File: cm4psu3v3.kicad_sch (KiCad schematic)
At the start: 26 parts, among them U12 AP64501SP-13

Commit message: respin
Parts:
- renumbered C30 to C32, C31 to C33, C32 to C34, C33 to C35, C34 to C36, C35 to C37, C36 to C38, C37 to C39, C38 to C40, C39 to C41, C40 to C42, C41 to C43, C42 to C44, C43 to C45, C44 to C46, C45 to C47, D9 to D8, R34 to R37, R35 to R38, R36 to R39, R37 to R40, R38 to R41, U12 to U13
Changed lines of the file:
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@@
   (symbol (lib_id "Device:C_Small") (at 168.91 160.02 0) (unit 1)
     (in_bom yes) (on_board yes)
-    (property "Reference" "C37" (id 0) (at 171.45 158.75 0)
+    (property "Reference" "C39" (id 0) (at 171.45 158.75 0)
       (effects (font (size 1.27 1.27)) (justify left))
     )
@@
   (symbol (lib_id "Device:C_Small") (at 121.92 151.13 0) (unit 1)
     (in_bom yes) (on_board yes)
-    (property "Reference" "C33" (id 0) (at 124.46 149.86 0)
+    (property "Reference" "C35" (id 0) (at 124.46 149.86 0)
       (effects (font (size 1.27 1.27)) (justify left))
     )
@@
   (symbol (lib_id "power:GND") (at 152.4 171.45 0) (unit 1)
     (in_bom yes) (on_board yes)
-    (property "Reference" "#PWR037" (id 0) (at 152.4 177.8 0)
+    (property "Reference" "#PWR038" (id 0) (at 152.4 177.8 0)
       (effects (font (size 1.27 1.27)) hide)
     )
@@
   (symbol (lib_id "Capacitor_Tantalum_SMD_MyOwn:CP_EIA-7343-31_Kemet-D") (at 292.1 134.62 0) (unit 1)
     (in_bom yes) (on_board yes)
-    (property "Reference" "C45" (id 0) (at 294.64 133.35 0)
+    (property "Reference" "C47" (id 0) (at 294.64 133.35 0)
       (effects (font (size 1.27 1.27)) (justify left))
     )
@@
   (symbol (lib_id "Device:C_Small") (at 158.75 134.62 0) (unit 1)
     (in_bom yes) (on_board yes)
-    (property "Reference" "C36" (id 0) (at 161.29 133.35 0)
+    (property "Reference" "C38" (id 0) (at 161.29 133.35 0)
       (effects (font (size 1.27 1.27)) (justify left))
     )
@@
   (symbol (lib_id "Device:R_Small") (at 219.71 160.02 0) (unit 1)
     (in_bom yes) (on_board yes)
-    (property "Reference" "R37" (id 0) (at 220.98 158.75 0)
+    (property "Reference" "R40" (id 0) (at 220.98 158.75 0)
       (effects (font (size 1.27 1.27)) (justify left))
     )
@@
   (symbol (lib_id "Device:C_Small") (at 243.84 134.62 0) (unit 1)
     (in_bom yes) (on_board yes)
-    (property "Reference" "C41" (id 0) (at 246.38 133.35 0)
+    (property "Reference" "C43" (id 0) (at 246.38 133.35 0)
       (effects (font (size 1.27 1.27)) (justify left))
     )
@@
   (symbol (lib_id "Device:R_Small") (at 170.18 128.27 270) (unit 1)
     (in_bom yes) (on_board yes)
-    (property "Reference" "R34" (id 0) (at 168.91 125.73 90)
+    (property "Reference" "R37" (id 0) (at 168.91 125.73 90)
       (effects (font (size 1.27 1.27)) (justify left))
     )
@@
   (symbol (lib_id "Device:C_Small") (at 255.27 134.62 0) (unit 1)
     (in_bom yes) (on_board yes)
-    (property "Reference" "C42" (id 0) (at 257.81 133.35 0)
+    (property "Reference" "C44" (id 0) (at 257.81 133.35 0)
       (effects (font (size 1.27 1.27)) (justify left))
     )
@@
   (symbol (lib_id "Device:C_Small") (at 278.13 134.62 0) (unit 1)
     (in_bom yes) (on_board yes)
-    (property "Reference" "C44" (id 0) (at 280.67 133.35 0)
+    (property "Reference" "C46" (id 0) (at 280.67 133.35 0)
       (effects (font (size 1.27 1.27)) (justify left))
     )
@@
   (symbol (lib_id "LED_SMD_LiteOn:LED Green") (at 307.975 143.51 270) (unit 1)
     (in_bom yes) (on_board yes)
-    (property "Reference" "D9" (id 0) (at 311.15 142.875 90))
+    (property "Reference" "D8" (id 0) (at 311.15 142.875 90))
     (property "Value" "LED Green" (id 1) (at 314.96 144.78 90))
     (property "Footprint" "LED_SMD_LiteOn:LED_0603_1608Metric_green" (id 2) (at 297.815 143.51 0)
@@
   (symbol (lib_id "Device:C_Small") (at 227.33 137.16 0) (unit 1)
     (in_bom no) (on_board no)
-    (property "Reference" "C40" (id 0) (at 229.87 135.89 0)
+    (property "Reference" "C42" (id 0) (at 229.87 135.89 0)
       (effects (font (size 1.27 1.27)) (justify left))
     )
@@
   (symbol (lib_id "power:GND") (at 292.1 171.45 0) (unit 1)
     (in_bom yes) (on_board yes)
-    (property "Reference" "#PWR041" (id 0) (at 292.1 177.8 0)
+    (property "Reference" "#PWR042" (id 0) (at 292.1 177.8 0)
       (effects (font (size 1.27 1.27)) hide)
     )
@@
   (symbol (lib_id "Device:R_Small") (at 307.975 134.62 0) (unit 1)
     (in_bom yes) (on_board yes)
-    (property "Reference" "R38" (id 0) (at 311.15 133.35 0))
+    (property "Reference" "R41" (id 0) (at 311.15 133.35 0))
     (property "Value" "1k" (id 1) (at 311.15 135.89 0))
     (property "Footprint" "Resistor_SMD:R_0402_1005Metric" (id 2) (at 307.975 134.62 0)
@@
   (symbol (lib_id "Device:R_Small") (at 208.28 156.21 0) (unit 1)
     (in_bom yes) (on_board yes)
-    (property "Reference" "R35" (id 0) (at 209.55 154.94 0)
+    (property "Reference" "R38" (id 0) (at 209.55 154.94 0)
       (effects (font (size 1.27 1.27)) (justify left))
     )
@@
   (symbol (lib_id "Device:C_Small") (at 91.44 151.13 0) (unit 1)
     (in_bom yes) (on_board yes)
-    (property "Reference" "C31" (id 0) (at 93.98 149.86 0)
+    (property "Reference" "C33" (id 0) (at 93.98 149.86 0)
       (effects (font (size 1.27 1.27)) (justify left))
     )
@@
   (symbol (lib_id "Device:C_Small") (at 208.28 163.83 0) (unit 1)
     (in_bom yes) (on_board yes)
-    (property "Reference" "C39" (id 0) (at 210.82 162.56 0)
+    (property "Reference" "C41" (id 0) (at 210.82 162.56 0)
       (effects (font (size 1.27 1.27)) (justify left))
     )
@@
   (symbol (lib_id "Device:C_Small") (at 76.2 151.13 0) (unit 1)
     (in_bom yes) (on_board yes)
-    (property "Reference" "C30" (id 0) (at 78.74 149.86 0)
+    (property "Reference" "C32" (id 0) (at 78.74 149.86 0)
       (effects (font (size 1.27 1.27)) (justify left))
     )
@@
   (symbol (lib_id "power:GND") (at 307.975 171.45 0) (unit 1)
     (in_bom yes) (on_board yes)
-    (property "Reference" "#PWR042" (id 0) (at 307.975 177.8 0)
+    (property "Reference" "#PWR043" (id 0) (at 307.975 177.8 0)
       (effects (font (size 1.27 1.27)) hide)
     )
@@
   (symbol (lib_id "Device:C_Small") (at 266.7 134.62 0) (unit 1)
     (in_bom yes) (on_board yes)
-    (property "Reference" "C43" (id 0) (at 269.24 133.35 0)
+    (property "Reference" "C45" (id 0) (at 269.24 133.35 0)
       (effects (font (size 1.27 1.27)) (justify left))
     )
@@
   (symbol (lib_id "Device:C_Small") (at 137.16 151.13 0) (unit 1)
     (in_bom yes) (on_board yes)
-    (property "Reference" "C34" (id 0) (at 139.7 149.86 0)
+    (property "Reference" "C36" (id 0) (at 139.7 149.86 0)
       (effects (font (size 1.27 1.27)) (justify left))
     )
@@
   (symbol (lib_id "power:GND") (at 278.13 171.45 0) (unit 1)
     (in_bom yes) (on_board yes)
-    (property "Reference" "#PWR040" (id 0) (at 278.13 177.8 0)
+    (property "Reference" "#PWR041" (id 0) (at 278.13 177.8 0)
       (effects (font (size 1.27 1.27)) hide)
     )
@@
   (symbol (lib_id "Device:R_Small") (at 212.09 137.16 0) (unit 1)
     (in_bom yes) (on_board yes)
-    (property "Reference" "R36" (id 0) (at 213.36 135.89 0)
+    (property "Reference" "R39" (id 0) (at 213.36 135.89 0)
       (effects (font (size 1.27 1.27)) (justify left))
     )
@@
   (symbol (lib_id "Regulator_Switching_Diodes:AP64501SP-13") (at 177.8 147.32 0) (unit 1)
     (in_bom yes) (on_board yes)
-    (property "Reference" "U12" (id 0) (at 177.165 137.16 0))
+    (property "Reference" "U13" (id 0) (at 177.165 137.16 0))
     (property "Value" "AP64501SP-13" (id 1) (at 177.8 139.7 0))
     (property "Footprint" "Regulator_Switching_Diodes:SOIC-8-1EP_3.9x4.9mm_P1.27mm_EP2.95x4.9mm_Mask2.71x3.4mm_ThermalVias" (id 2) (at 177.8 172.72 0)
@@
   (symbol (lib_id "Device:C_Small") (at 106.68 151.13 0) (unit 1)
     (in_bom yes) (on_board yes)
-    (property "Reference" "C32" (id 0) (at 109.22 149.86 0)
+    (property "Reference" "C34" (id 0) (at 109.22 149.86 0)
       (effects (font (size 1.27 1.27)) (justify left))
     )
@@
   (symbol (lib_id "power:GND") (at 251.46 171.45 0) (unit 1)
     (in_bom yes) (on_board yes)
-    (property "Reference" "#PWR039" (id 0) (at 251.46 177.8 0)
+    (property "Reference" "#PWR040" (id 0) (at 251.46 177.8 0)
       (effects (font (size 1.27 1.27)) hide)
     )
@@
   (symbol (lib_id "Device:C_Small") (at 196.85 160.02 0) (unit 1)
     (in_bom yes) (on_board yes)
-    (property "Reference" "C38" (id 0) (at 199.39 158.75 0)
+    (property "Reference" "C40" (id 0) (at 199.39 158.75 0)
       (effects (font (size 1.27 1.27)) (justify left))
     )
@@
   (symbol (lib_id "power:GND") (at 219.71 171.45 0) (unit 1)
     (in_bom yes) (on_board yes)
-    (property "Reference" "#PWR038" (id 0) (at 219.71 177.8 0)
+    (property "Reference" "#PWR039" (id 0) (at 219.71 177.8 0)
       (effects (font (size 1.27 1.27)) hide)
     )
@@
   (symbol (lib_id "Device:C_Small") (at 152.4 151.13 0) (unit 1)
     (in_bom yes) (on_board yes)
-    (property "Reference" "C35" (id 0) (at 154.94 149.86 0)
-      (effects (font (size 1.27 1.27)) (justify left))
-    )
+    (property "Reference" "C37" (id 0) (at 154.94 149.86 0)
+      (effects (font (size 1.27 1.27)) (justify left))
+    )

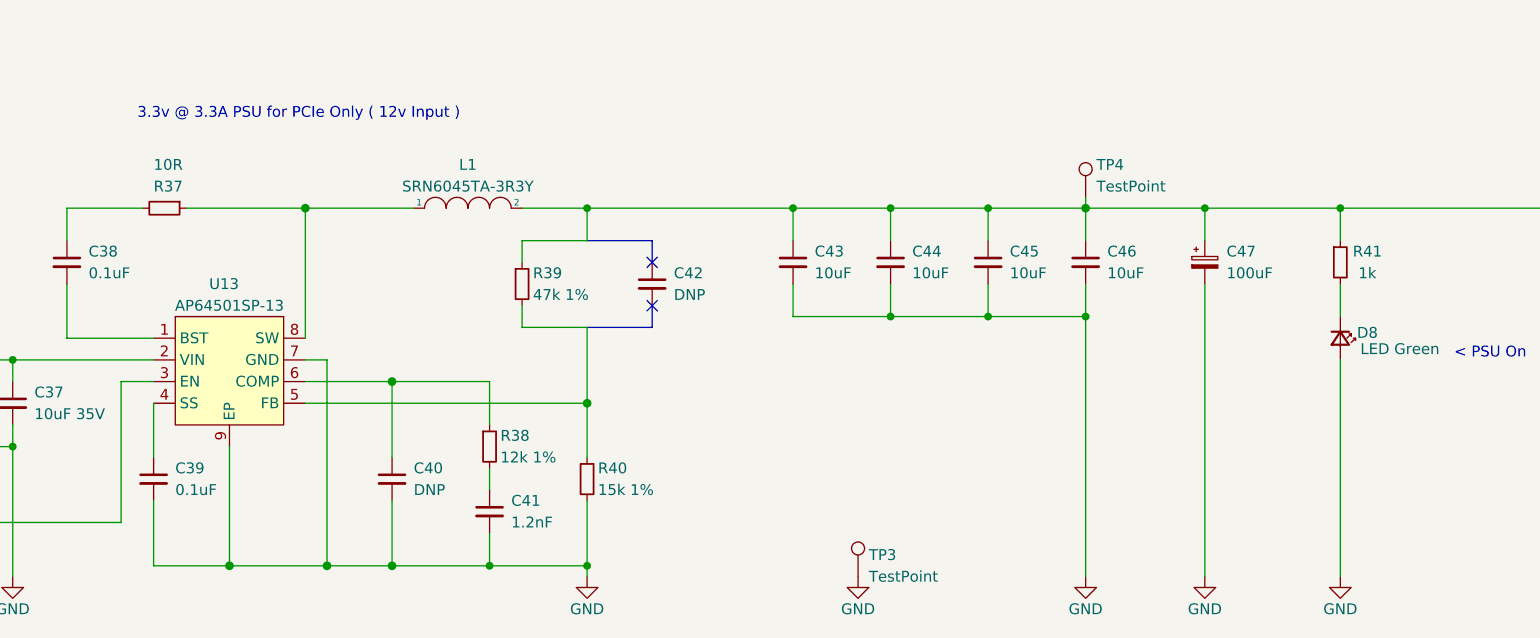
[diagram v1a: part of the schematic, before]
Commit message: fixed I2C ping indicator
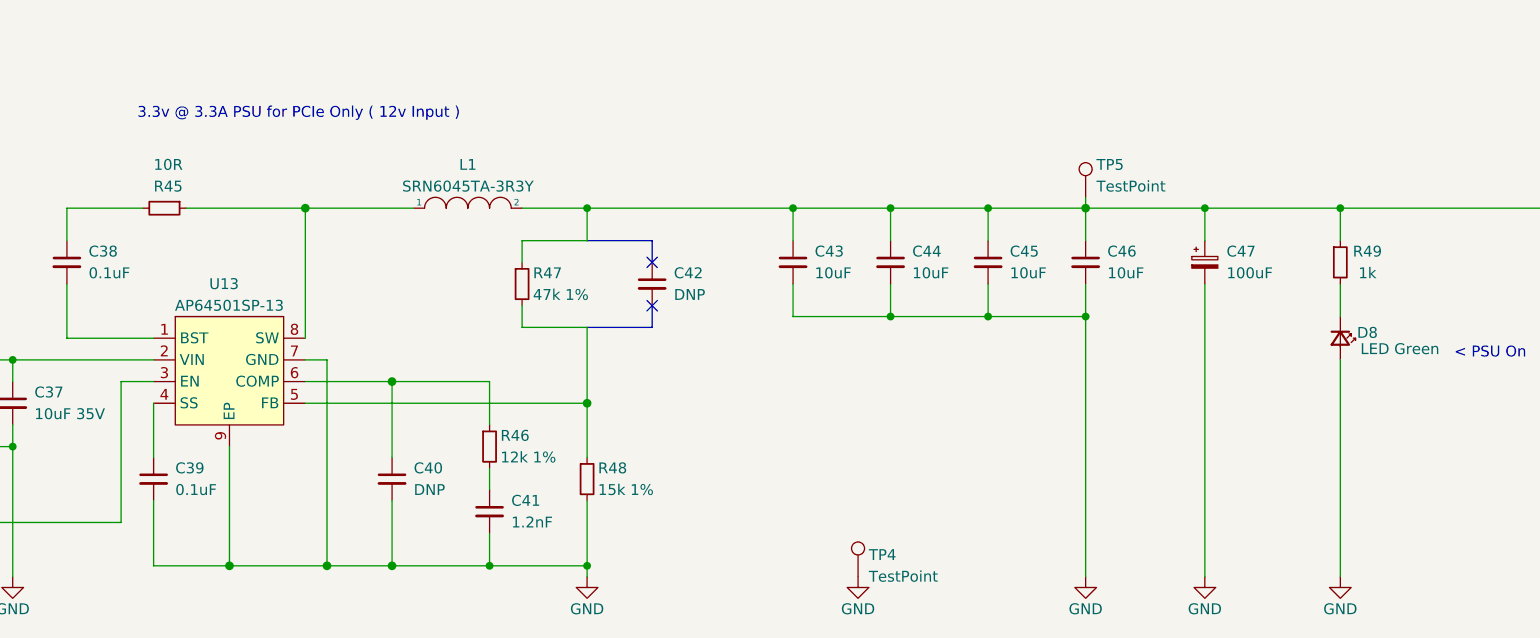
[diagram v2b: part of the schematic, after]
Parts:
- renumbered R37 to R45, R38 to R46, R39 to R47, R40 to R48, R41 to R49, TP3 to TP4, TP4 to TP5
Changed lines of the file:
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@@
   (symbol (lib_id "power:GND") (at 152.4 171.45 0) (unit 1)
     (in_bom yes) (on_board yes)
-    (property "Reference" "#PWR038" (id 0) (at 152.4 177.8 0)
+    (property "Reference" "#PWR040" (id 0) (at 152.4 177.8 0)
       (effects (font (size 1.27 1.27)) hide)
     )
@@
   (symbol (lib_id "Connector:TestPoint") (at 251.46 171.45 0) (unit 1)
     (in_bom yes) (on_board yes)
-    (property "Reference" "TP3" (id 0) (at 252.73 168.91 0)
+    (property "Reference" "TP4" (id 0) (at 252.73 168.91 0)
       (effects (font (size 1.27 1.27)) (justify left))
     )
@@
   (symbol (lib_id "Device:R_Small") (at 219.71 160.02 0) (unit 1)
     (in_bom yes) (on_board yes)
-    (property "Reference" "R40" (id 0) (at 220.98 158.75 0)
+    (property "Reference" "R48" (id 0) (at 220.98 158.75 0)
       (effects (font (size 1.27 1.27)) (justify left))
     )
@@
   (symbol (lib_id "Device:R_Small") (at 170.18 128.27 270) (unit 1)
     (in_bom yes) (on_board yes)
-    (property "Reference" "R37" (id 0) (at 168.91 125.73 90)
+    (property "Reference" "R45" (id 0) (at 168.91 125.73 90)
       (effects (font (size 1.27 1.27)) (justify left))
     )
@@
   (symbol (lib_id "power:GND") (at 292.1 171.45 0) (unit 1)
     (in_bom yes) (on_board yes)
-    (property "Reference" "#PWR042" (id 0) (at 292.1 177.8 0)
+    (property "Reference" "#PWR044" (id 0) (at 292.1 177.8 0)
       (effects (font (size 1.27 1.27)) hide)
     )
@@
   (symbol (lib_id "Device:R_Small") (at 307.975 134.62 0) (unit 1)
     (in_bom yes) (on_board yes)
-    (property "Reference" "R41" (id 0) (at 311.15 133.35 0))
+    (property "Reference" "R49" (id 0) (at 311.15 133.35 0))
     (property "Value" "1k" (id 1) (at 311.15 135.89 0))
     (property "Footprint" "Resistor_SMD:R_0402_1005Metric" (id 2) (at 307.975 134.62 0)
@@
   (symbol (lib_id "Device:R_Small") (at 208.28 156.21 0) (unit 1)
     (in_bom yes) (on_board yes)
-    (property "Reference" "R38" (id 0) (at 209.55 154.94 0)
+    (property "Reference" "R46" (id 0) (at 209.55 154.94 0)
       (effects (font (size 1.27 1.27)) (justify left))
     )
@@
   (symbol (lib_id "power:GND") (at 307.975 171.45 0) (unit 1)
     (in_bom yes) (on_board yes)
-    (property "Reference" "#PWR043" (id 0) (at 307.975 177.8 0)
+    (property "Reference" "#PWR045" (id 0) (at 307.975 177.8 0)
       (effects (font (size 1.27 1.27)) hide)
     )
@@
   (symbol (lib_id "power:GND") (at 278.13 171.45 0) (unit 1)
     (in_bom yes) (on_board yes)
-    (property "Reference" "#PWR041" (id 0) (at 278.13 177.8 0)
+    (property "Reference" "#PWR043" (id 0) (at 278.13 177.8 0)
       (effects (font (size 1.27 1.27)) hide)
     )
@@
   (symbol (lib_id "Device:R_Small") (at 212.09 137.16 0) (unit 1)
     (in_bom yes) (on_board yes)
-    (property "Reference" "R39" (id 0) (at 213.36 135.89 0)
+    (property "Reference" "R47" (id 0) (at 213.36 135.89 0)
       (effects (font (size 1.27 1.27)) (justify left))
     )
@@
   (symbol (lib_id "Connector:TestPoint") (at 278.13 127 0) (unit 1)
     (in_bom yes) (on_board yes)
-    (property "Reference" "TP4" (id 0) (at 279.4 123.19 0)
+    (property "Reference" "TP5" (id 0) (at 279.4 123.19 0)
       (effects (font (size 1.27 1.27)) (justify left))
     )
@@
   (symbol (lib_id "power:GND") (at 251.46 171.45 0) (unit 1)
     (in_bom yes) (on_board yes)
-    (property "Reference" "#PWR040" (id 0) (at 251.46 177.8 0)
+    (property "Reference" "#PWR042" (id 0) (at 251.46 177.8 0)
       (effects (font (size 1.27 1.27)) hide)
     )
@@
   (symbol (lib_id "power:GND") (at 219.71 171.45 0) (unit 1)
     (in_bom yes) (on_board yes)
-    (property "Reference" "#PWR039" (id 0) (at 219.71 177.8 0)
-      (effects (font (size 1.27 1.27)) hide)
-    )
+    (property "Reference" "#PWR041" (id 0) (at 219.71 177.8 0)
+      (effects (font (size 1.27 1.27)) hide)
+    )
